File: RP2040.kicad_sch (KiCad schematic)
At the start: 21 parts, among them U3 RP2040, Y1 12MHz

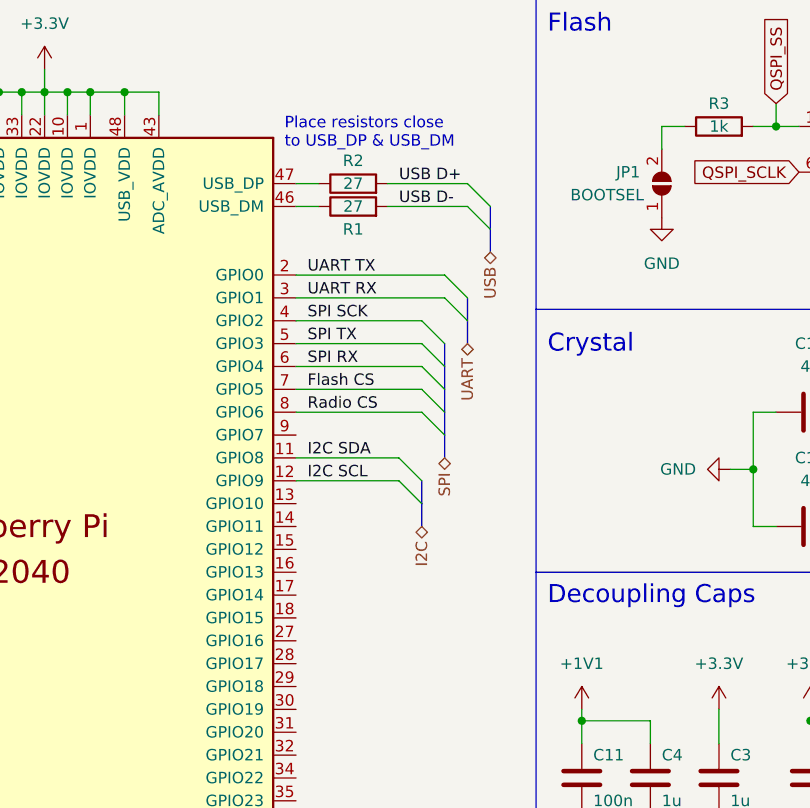
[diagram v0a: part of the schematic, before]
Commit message: Fixed bus names
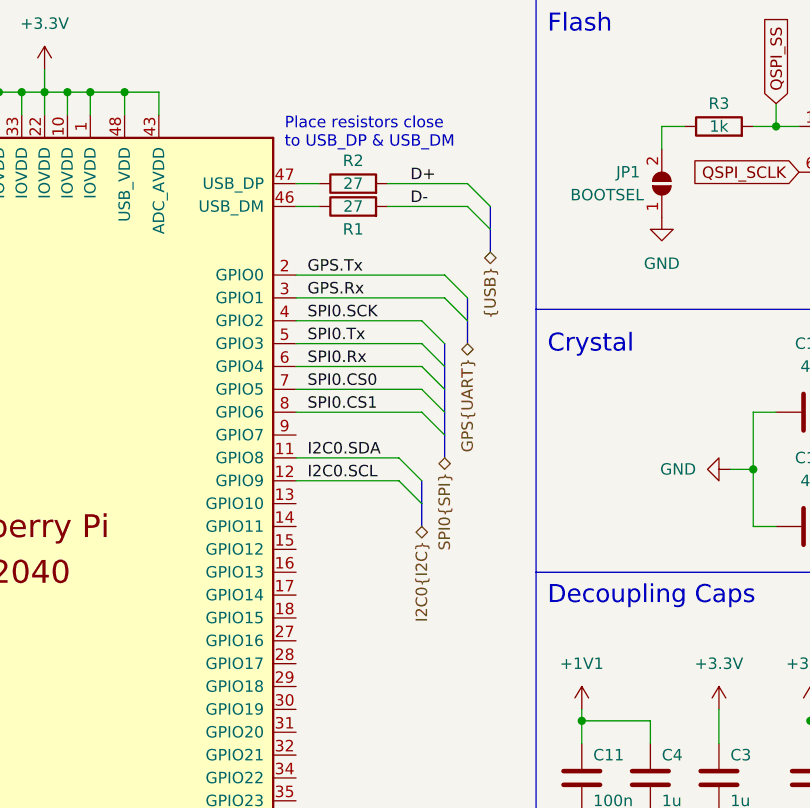
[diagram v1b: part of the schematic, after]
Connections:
- net Flash CS renamed SPI0.CS0
- net I2C SCL renamed I2C0.SCL
- net I2C SDA renamed I2C0.SDA
- net Radio CS renamed SPI0.CS1
- net SPI RX renamed SPI0.Rx
- net SPI SCK renamed SPI0.SCK
- net SPI TX renamed SPI0.Tx
- net UART RX renamed GPS.Rx
- net UART TX renamed GPS.Tx
- net USB D+ renamed D+
- net USB D- renamed D-

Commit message: Various updates because I forgot to commit for a while
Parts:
- renumbered C11 to C1, C8 to C10, C18 to C11, C4 to C2, C10 to C4, C13 to C5, C9 to C6, C1 to C7, C7 to C8, C12 to C9, JP2 to JP1, JP1 to JP2, R4 to R3, R2 to R4, R1 to R5, R3 to R6, R5 to R7, U3 to U1, U1 to U2
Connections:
- net Accel1: now reaches U1.13 (GPIO10)
- net Accel2: now reaches U1.14 (GPIO11)
- net Gyro1: now reaches U1.15 (GPIO12)
- net Gyro2: now reaches U1.16 (GPIO13)
- net Pyro1: now reaches U1.17 (GPIO14)
- net Pyro2: now reaches U1.18 (GPIO15)
- net Pyro3: now reaches U1.27 (GPIO16)
- net Pyro4: now reaches U1.28 (GPIO17)
- net Cont1: now reaches U1.29 (GPIO18)
- net Cont2: now reaches U1.30 (GPIO19)
- net Cont3: now reaches U1.31 (GPIO20)
- net Cont4: now reaches U1.32 (GPIO21)
- net GPIO22: now reaches U1.34 (GPIO22)
- net GPIO23: now reaches U1.35 (GPIO23)
- net GPIO24: now reaches U1.36 (GPIO24)
- net GPIO25: now reaches U1.37 (GPIO25)
- net ADC0: now reaches U1.38 (GPIO26_ADC0)
- net ADC1: now reaches U1.39 (GPIO27_ADC1)
- net ADC2: now reaches U1.40 (GPIO28_ADC2)
- net ADC: now reaches U1.41 (GPIO29_ADC3)

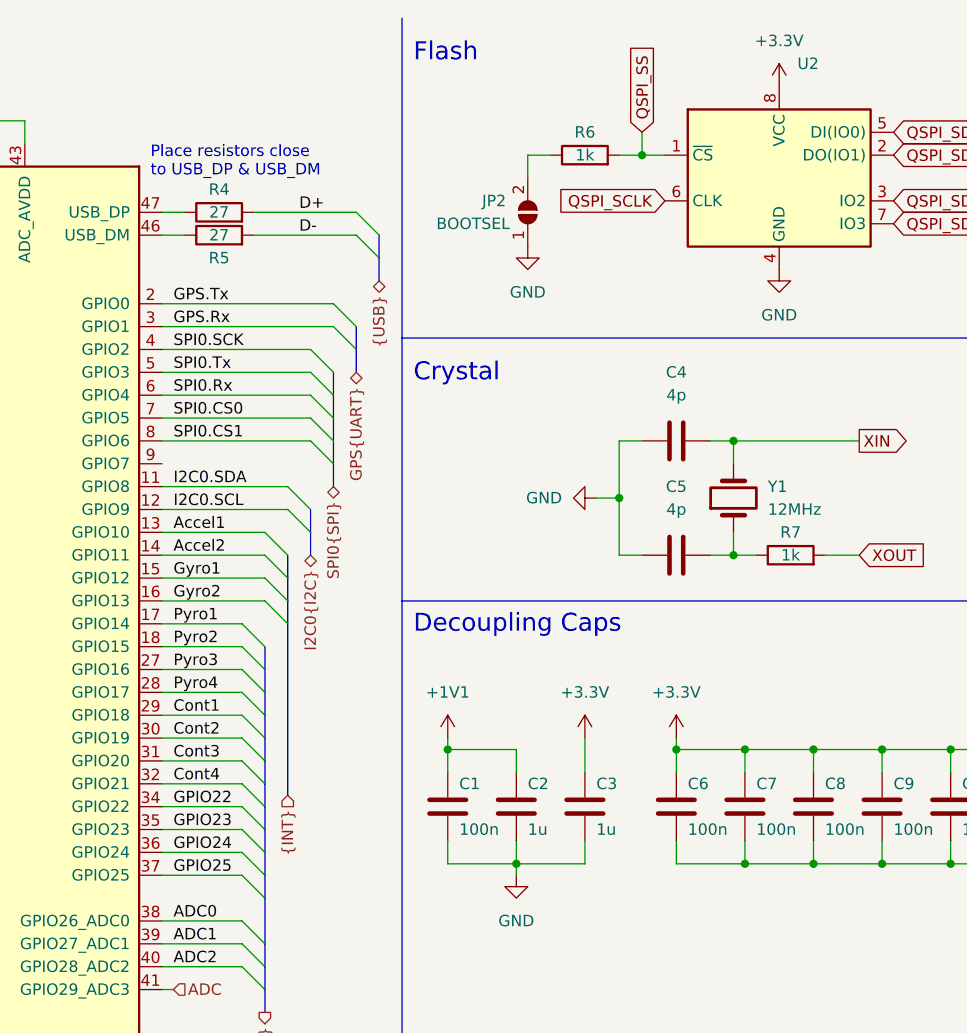
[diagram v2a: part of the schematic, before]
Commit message: Connected the sensors, flash chip, Need to connect the radio and GPS
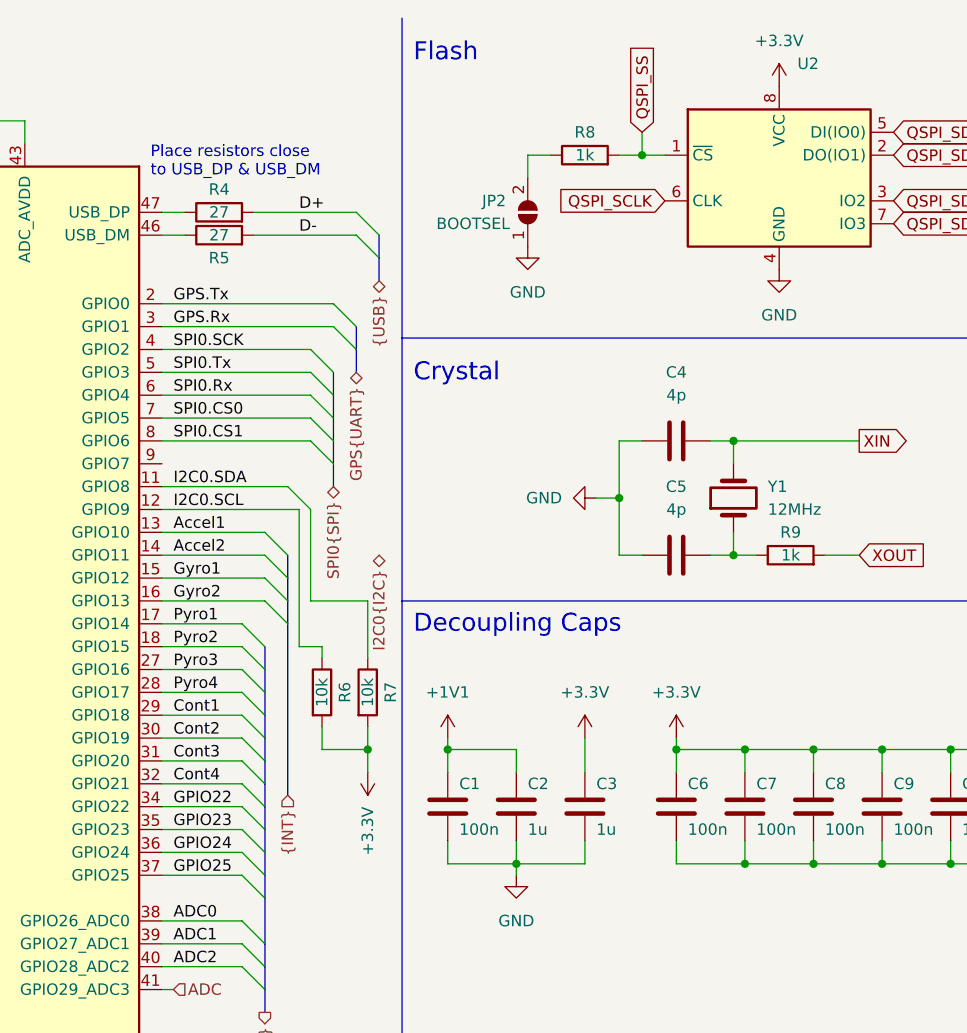
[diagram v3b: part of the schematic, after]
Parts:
- added R6, R7: 10k, Resistor_SMD:R_0603_1608Metric, symbol Device:R
- renumbered R6 to R8, R7 to R9
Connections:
- net +3V3: now also R6.2, R7.2
- net I2C0.SCL: now also R6.1
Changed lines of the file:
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@@
   (junction (at 175.26 105.41) (diameter 0) (color 0 0 0 0)
   )
+  (junction (at 118.11 92.71) (diameter 0) (color 0 0 0 0)
+  )
   (junction (at 127 92.71) (diameter 0) (color 0 0 0 0)
   )
@@
     (stroke (width 0) (type default) (color 0 0 0 0))
   )
-  (bus_entry (at 111.76 68.58) (size -2.54 -2.54)
-    (stroke (width 0) (type default) (color 0 0 0 0))
-  )
   (bus_entry (at 114.3 60.96) (size -2.54 -2.54)
     (stroke (width 0) (type default) (color 0 0 0 0))
@@
     (stroke (width 0) (type default) (color 0 0 0 0))
   )
+  (wire (pts (xy 113.03 81.28) (xy 113.03 82.55))
+    (stroke (width 0) (type default) (color 0 0 0 0))
+  )
   (wire (pts (xy 182.88 105.41) (xy 190.5 105.41))
     (stroke (width 0) (type default) (color 0 0 0 0))
@@
     (stroke (width 0) (type default) (color 0 0 0 0))
   )
+  (wire (pts (xy 111.76 76.2) (xy 118.11 76.2))
+    (stroke (width 0) (type default) (color 0 0 0 0))
+  )
   (bus (pts (xy 106.68 99.06) (xy 106.68 101.6))
     (stroke (width 0) (type default) (color 0 0 0 0))
@@
     (stroke (width 0) (type default) (color 0 0 0 0))
   )
+  (wire (pts (xy 118.11 92.71) (xy 113.03 92.71))
+    (stroke (width 0) (type default) (color 0 0 0 0))
+  )
   (wire (pts (xy 142.24 105.41) (xy 142.24 102.87))
     (stroke (width 0) (type default) (color 0 0 0 0))
@@
     (stroke (width 0) (type default) (color 0 0 0 0))
   )
+  (wire (pts (xy 110.49 66.04) (xy 110.49 81.28))
+    (stroke (width 0) (type default) (color 0 0 0 0))
+  )
   (wire (pts (xy 16.51 83.82) (xy 16.51 86.36))
     (stroke (width 0) (type default) (color 0 0 0 0))
@@
     (stroke (width 0) (type default) (color 0 0 0 0))
   )
+  (wire (pts (xy 113.03 92.71) (xy 113.03 90.17))
+    (stroke (width 0) (type default) (color 0 0 0 0))
+  )
   (polyline (pts (xy 121.92 46.99) (xy 198.12 46.99))
     (stroke (width 0) (type default) (color 0 0 0 0))
@@
     (stroke (width 0) (type default) (color 0 0 0 0))
   )
+  (wire (pts (xy 111.76 66.04) (xy 111.76 76.2))
+    (stroke (width 0) (type default) (color 0 0 0 0))
+  )
   (wire (pts (xy 95.25 83.82) (xy 104.14 83.82))
     (stroke (width 0) (type default) (color 0 0 0 0))
@@
     (stroke (width 0) (type default) (color 0 0 0 0))
   )
+  (wire (pts (xy 118.11 90.17) (xy 118.11 92.71))
+    (stroke (width 0) (type default) (color 0 0 0 0))
+  )
+  (wire (pts (xy 110.49 81.28) (xy 113.03 81.28))
+    (stroke (width 0) (type default) (color 0 0 0 0))
+  )
   (wire (pts (xy 127 91.44) (xy 127 92.71))
     (stroke (width 0) (type default) (color 0 0 0 0))
   )
-  (wire (pts (xy 95.25 66.04) (xy 109.22 66.04))
+  (wire (pts (xy 95.25 66.04) (xy 110.49 66.04))
     (stroke (width 0) (type default) (color 0 0 0 0))
   )
@@
     (stroke (width 0) (type default) (color 0 0 0 0))
   )
+  (wire (pts (xy 118.11 92.71) (xy 118.11 95.25))
+    (stroke (width 0) (type default) (color 0 0 0 0))
+  )
   (wire (pts (xy 175.26 105.41) (xy 182.88 105.41))
     (stroke (width 0) (type default) (color 0 0 0 0))
@@
     (stroke (width 0) (type default) (color 0 0 0 0))
   )
-  (bus (pts (xy 111.76 68.58) (xy 111.76 71.12))
-    (stroke (width 0) (type default) (color 0 0 0 0))
-  )
   (wire (pts (xy 95.25 68.58) (xy 106.68 68.58))
     (stroke (width 0) (type default) (color 0 0 0 0))
@@
     (stroke (width 0) (type default) (color 0 0 0 0))
   )
+  (wire (pts (xy 118.11 76.2) (xy 118.11 82.55))
+    (stroke (width 0) (type default) (color 0 0 0 0))
+  )
   (bus (pts (xy 109.22 71.12) (xy 109.22 73.66))
     (stroke (width 0) (type default) (color 0 0 0 0))
@@
   )
   (bus (pts (xy 106.68 96.52) (xy 106.68 99.06))
-    (stroke (width 0) (type default) (color 0 0 0 0))
-  )
-  (bus (pts (xy 111.76 66.04) (xy 111.76 68.58))
     (stroke (width 0) (type default) (color 0 0 0 0))
   )
@@
     (effects (font (size 1.27 1.27)) (justify right))
   )
-  (hierarchical_label "I2C0{I2C}" (shape bidirectional) (at 111.76 71.12 270)
+  (hierarchical_label "I2C0{I2C}" (shape bidirectional) (at 119.38 71.12 270)
     (effects (font (size 1.27 1.27)) (justify right))
   )
@@
   (symbol (lib_id "power:GND") (at 190.5 106.68 0) (unit 1)
     (in_bom yes) (on_board yes) (fields_autoplaced)
-    (property "Reference" "#PWR016" (id 0) (at 190.5 113.03 0)
+    (property "Reference" "#PWR017" (id 0) (at 190.5 113.03 0)
       (effects (font (size 1.27 1.27)) hide)
     )
@@
   (symbol (lib_id "power:+3.3V") (at 152.4 91.44 0) (unit 1)
     (in_bom yes) (on_board yes) (fields_autoplaced)
-    (property "Reference" "#PWR013" (id 0) (at 152.4 95.25 0)
+    (property "Reference" "#PWR014" (id 0) (at 152.4 95.25 0)
       (effects (font (size 1.27 1.27)) hide)
     )
@@
     (pin "1")
   )
+  (symbol (lib_id "Device:R") (at 113.03 86.36 0) (unit 1)
+    (in_bom yes) (on_board yes)
+    (property "Reference" "R6" (id 0) (at 115.57 86.36 90))
+    (property "Value" "10k" (id 1) (at 113.03 86.36 90))
+    (property "Footprint" "Resistor_SMD:R_0603_1608Metric" (id 2) (at 111.252 86.36 90)
+      (effects (font (size 1.27 1.27)) hide)
+    )
+    (property "Datasheet" "~" (id 3) (at 113.03 86.36 0)
+      (effects (font (size 1.27 1.27)) hide)
+    )
+    (pin "1")
+    (pin "2")
+  )
   (symbol (lib_id "Device:R") (at 165.1 71.12 90) (unit 1)
     (in_bom yes) (on_board yes)
-    (property "Reference" "R7" (id 0) (at 165.1 68.58 90))
+    (property "Reference" "R9" (id 0) (at 165.1 68.58 90))
     (property "Value" "1k" (id 1) (at 165.1 71.12 90))
     (property "Footprint" "Resistor_SMD:R_0603_1608Metric" (id 2) (at 165.1 72.898 90)
@@
   (symbol (lib_id "power:+3.3V") (at 163.83 19.05 0) (unit 1)
     (in_bom yes) (on_board yes) (fields_autoplaced)
-    (property "Reference" "#PWR014" (id 0) (at 163.83 22.86 0)
+    (property "Reference" "#PWR015" (id 0) (at 163.83 22.86 0)
       (effects (font (size 1.27 1.27)) hide)
     )
@@
   (symbol (lib_id "power:GND") (at 135.89 36.83 0) (unit 1)
     (in_bom yes) (on_board yes) (fields_autoplaced)
-    (property "Reference" "#PWR010" (id 0) (at 135.89 43.18 0)
+    (property "Reference" "#PWR011" (id 0) (at 135.89 43.18 0)
       (effects (font (size 1.27 1.27)) hide)
     )
@@
   (symbol (lib_id "power:GND") (at 163.83 39.37 0) (unit 1)
     (in_bom yes) (on_board yes) (fields_autoplaced)
-    (property "Reference" "#PWR015" (id 0) (at 163.83 45.72 0)
+    (property "Reference" "#PWR016" (id 0) (at 163.83 45.72 0)
       (effects (font (size 1.27 1.27)) hide)
     )
@@
   (symbol (lib_id "Device:R") (at 142.24 26.67 90) (unit 1)
     (in_bom yes) (on_board yes)
-    (property "Reference" "R6" (id 0) (at 142.24 24.13 90))
+    (property "Reference" "R8" (id 0) (at 142.24 24.13 90))
     (property "Value" "1k" (id 1) (at 142.24 26.67 90))
     (property "Footprint" "Resistor_SMD:R_0603_1608Metric" (id 2) (at 142.24 28.448 90)
@@
   (symbol (lib_id "power:+1V1") (at 127 91.44 0) (unit 1)
     (in_bom yes) (on_board yes)
-    (property "Reference" "#PWR08" (id 0) (at 127 95.25 0)
+    (property "Reference" "#PWR09" (id 0) (at 127 95.25 0)
       (effects (font (size 1.27 1.27)) hide)
     )
@@
     (pin "1")
   )
+  (symbol (lib_id "Device:R") (at 118.11 86.36 0) (unit 1)
+    (in_bom yes) (on_board yes)
+    (property "Reference" "R7" (id 0) (at 120.65 86.36 90))
+    (property "Value" "10k" (id 1) (at 118.11 86.36 90))
+    (property "Footprint" "Resistor_SMD:R_0603_1608Metric" (id 2) (at 116.332 86.36 90)
+      (effects (font (size 1.27 1.27)) hide)
+    )
+    (property "Datasheet" "~" (id 3) (at 118.11 86.36 0)
+      (effects (font (size 1.27 1.27)) hide)
+    )
+    (pin "1")
+    (pin "2")
+  )
   (symbol (lib_id "power:GND") (at 50.8 127 0) (unit 1)
     (in_bom yes) (on_board yes) (fields_autoplaced)
@@
   (symbol (lib_id "power:GND") (at 143.51 64.77 270) (unit 1)
     (in_bom yes) (on_board yes) (fields_autoplaced)
-    (property "Reference" "#PWR012" (id 0) (at 137.16 64.77 0)
+    (property "Reference" "#PWR013" (id 0) (at 137.16 64.77 0)
       (effects (font (size 1.27 1.27)) hide)
     )
@@
     (pin "2")
   )
+  (symbol (lib_id "power:+3.3V") (at 118.11 95.25 180) (unit 1)
+    (in_bom yes) (on_board yes) (fields_autoplaced)
+    (property "Reference" "#PWR08" (id 0) (at 118.11 91.44 0)
+      (effects (font (size 1.27 1.27)) hide)
+    )
+    (property "Value" "+3.3V" (id 1) (at 118.1101 99.06 90)
+      (effects (font (size 1.27 1.27)) (justify left))
+    )
+    (property "Footprint" "" (id 2) (at 118.11 95.25 0)
+      (effects (font (size 1.27 1.27)) hide)
+    )
+    (property "Datasheet" "" (id 3) (at 118.11 95.25 0)
+      (effects (font (size 1.27 1.27)) hide)
+    )
+    (pin "1")
+  )
   (symbol (lib_id "Device:Crystal") (at 158.75 64.77 90) (unit 1)
     (in_bom yes) (on_board yes) (fields_autoplaced)
@@
   (symbol (lib_id "power:GND") (at 134.62 106.68 0) (unit 1)
     (in_bom yes) (on_board yes) (fields_autoplaced)
-    (property "Reference" "#PWR09" (id 0) (at 134.62 113.03 0)
+    (property "Reference" "#PWR010" (id 0) (at 134.62 113.03 0)
       (effects (font (size 1.27 1.27)) hide)
     )
@@
   (symbol (lib_id "power:+3.3V") (at 142.24 91.44 0) (unit 1)
     (in_bom yes) (on_board yes) (fields_autoplaced)
-    (property "Reference" "#PWR011" (id 0) (at 142.24 95.25 0)
-      (effects (font (size 1.27 1.27)) hide)
-    )
+    (property "Reference" "#PWR012" (id 0) (at 142.24 95.25 0)
+      (effects (font (size 1.27 1.27)) hide)
+    )
